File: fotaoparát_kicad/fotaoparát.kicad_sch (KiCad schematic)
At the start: 22 parts, among them J1 Conn_01x08_Pin, SW1 SW_MEC_5G, SW2 SW_MEC_5G, U1 TLV62569DBV, Y2 Crystal_GND23

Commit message: FInalni doteky. Ted uz jenom opravy {snad}
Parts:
- Y2: value Crystal_GND23 -> Crystal_GND24; LSCS Number (none) -> C5544483
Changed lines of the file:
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@@
 			)
 		)
-		(property "Value" "Crystal_GND23"
+		(property "Value" "Crystal_GND24"
 			(at 162.306 30.48 0)
 			(effects
@@
 			(at 148.59 29.21 0)
 			(effects
+				(font
+					(size 1.27 1.27)
+				)
+				(hide yes)
+			)
+		)
+		(property "LSCS Number" "C5544483"
+			(at 148.59 29.21 0)
+			(effects

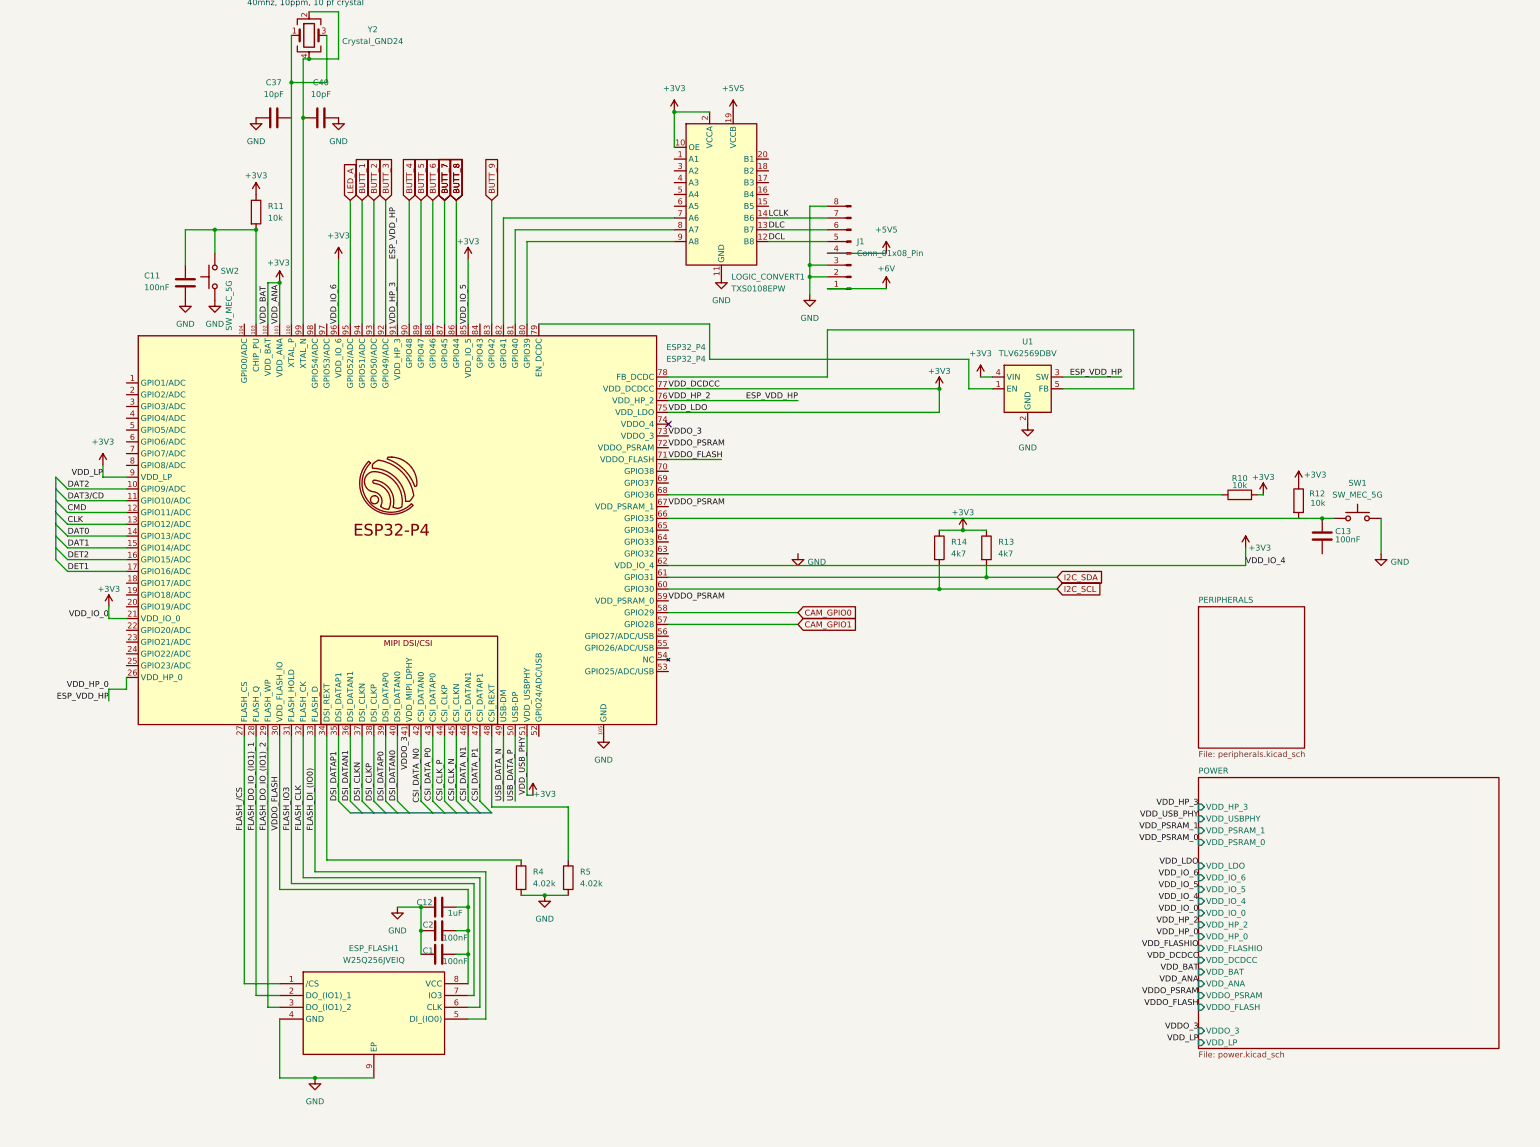
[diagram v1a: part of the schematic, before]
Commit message: Udelal jsem: -Predelani labelu na global -Pridani vyvodu na desku pro spoust -Pokusil se predelat ten stepdown, Vout by mela byt 1V1, nestihl jsem prepsat vsechny hodnoty a pridat lscs cisla
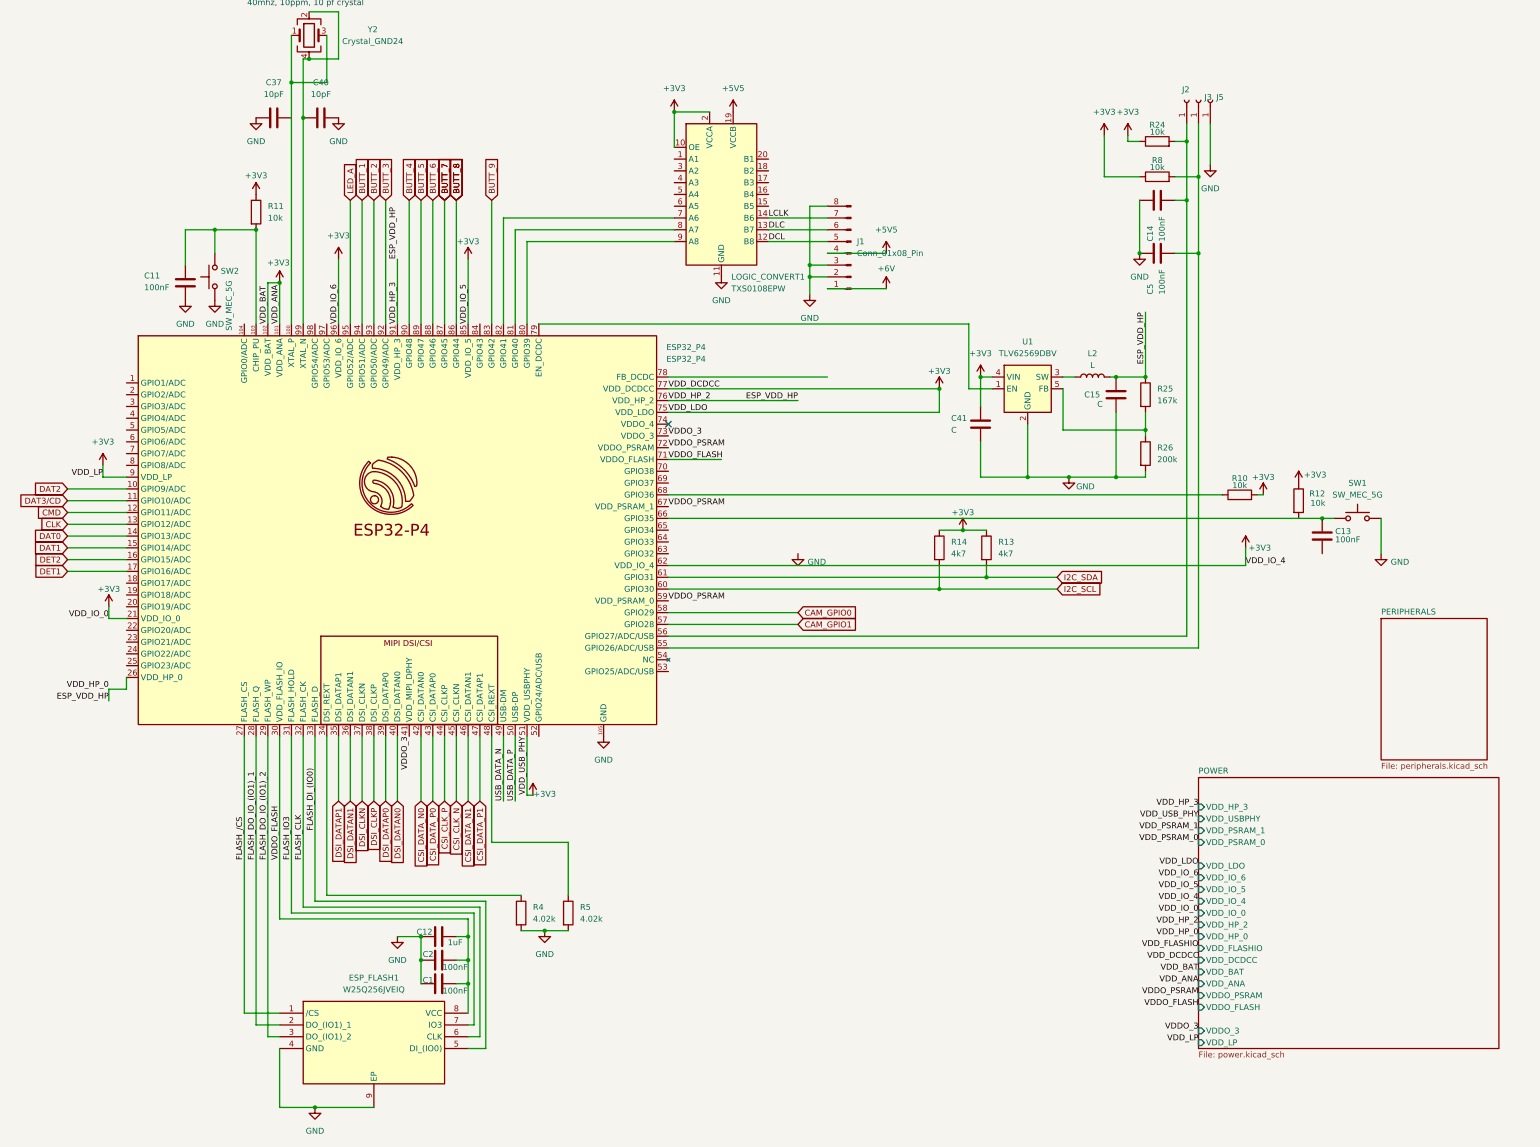
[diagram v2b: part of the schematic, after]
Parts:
- added C14, C5: 100nF, Capacitor_SMD:C_0201_0603Metric, symbol Device:C
- added C15, C41: C, symbol Device:C
- added J2, J3, J5: Conn_01x01_Socket, Connector_Wire:SolderWirePad_1x01_SMD_1.5x3mm, symbol Connector:Conn_01x01_Socket
- added L2: L, symbol Device:L
- added R24, R8: 10k, Resistor_SMD:R_0603_1608Metric, symbol Device:R
- added R25: 167k, symbol Device:R
- added R26: 200k, symbol Device:R
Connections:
- net +3V3: now also C41.1, R24.1, R8.1
- net ESP_VDD_HP: now also C15.1, L2.2, R25.1; no longer U1.3 (SW)
- net GND: now also C14.1, C15.2, C41.2, C5.1, J5.1 (Pin_1), R26.2
- net at ESP32_P4.55 (GPIO26/ADC/USB): now also C5.2, J3.1 (Pin_1), R8.2
- net at ESP32_P4.56 (GPIO27/ADC/USB): now also C14.2, J2.1 (Pin_1), R24.2
- net at U1.5 (FB): now also R25.2, R26.1; no longer ESP32_P4.78 (FB_DCDC)
- new net: L2.1, U1.3 (SW)
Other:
- moved on the sheet: C1, C12, C2, ESP_FLASH1, R4, R5

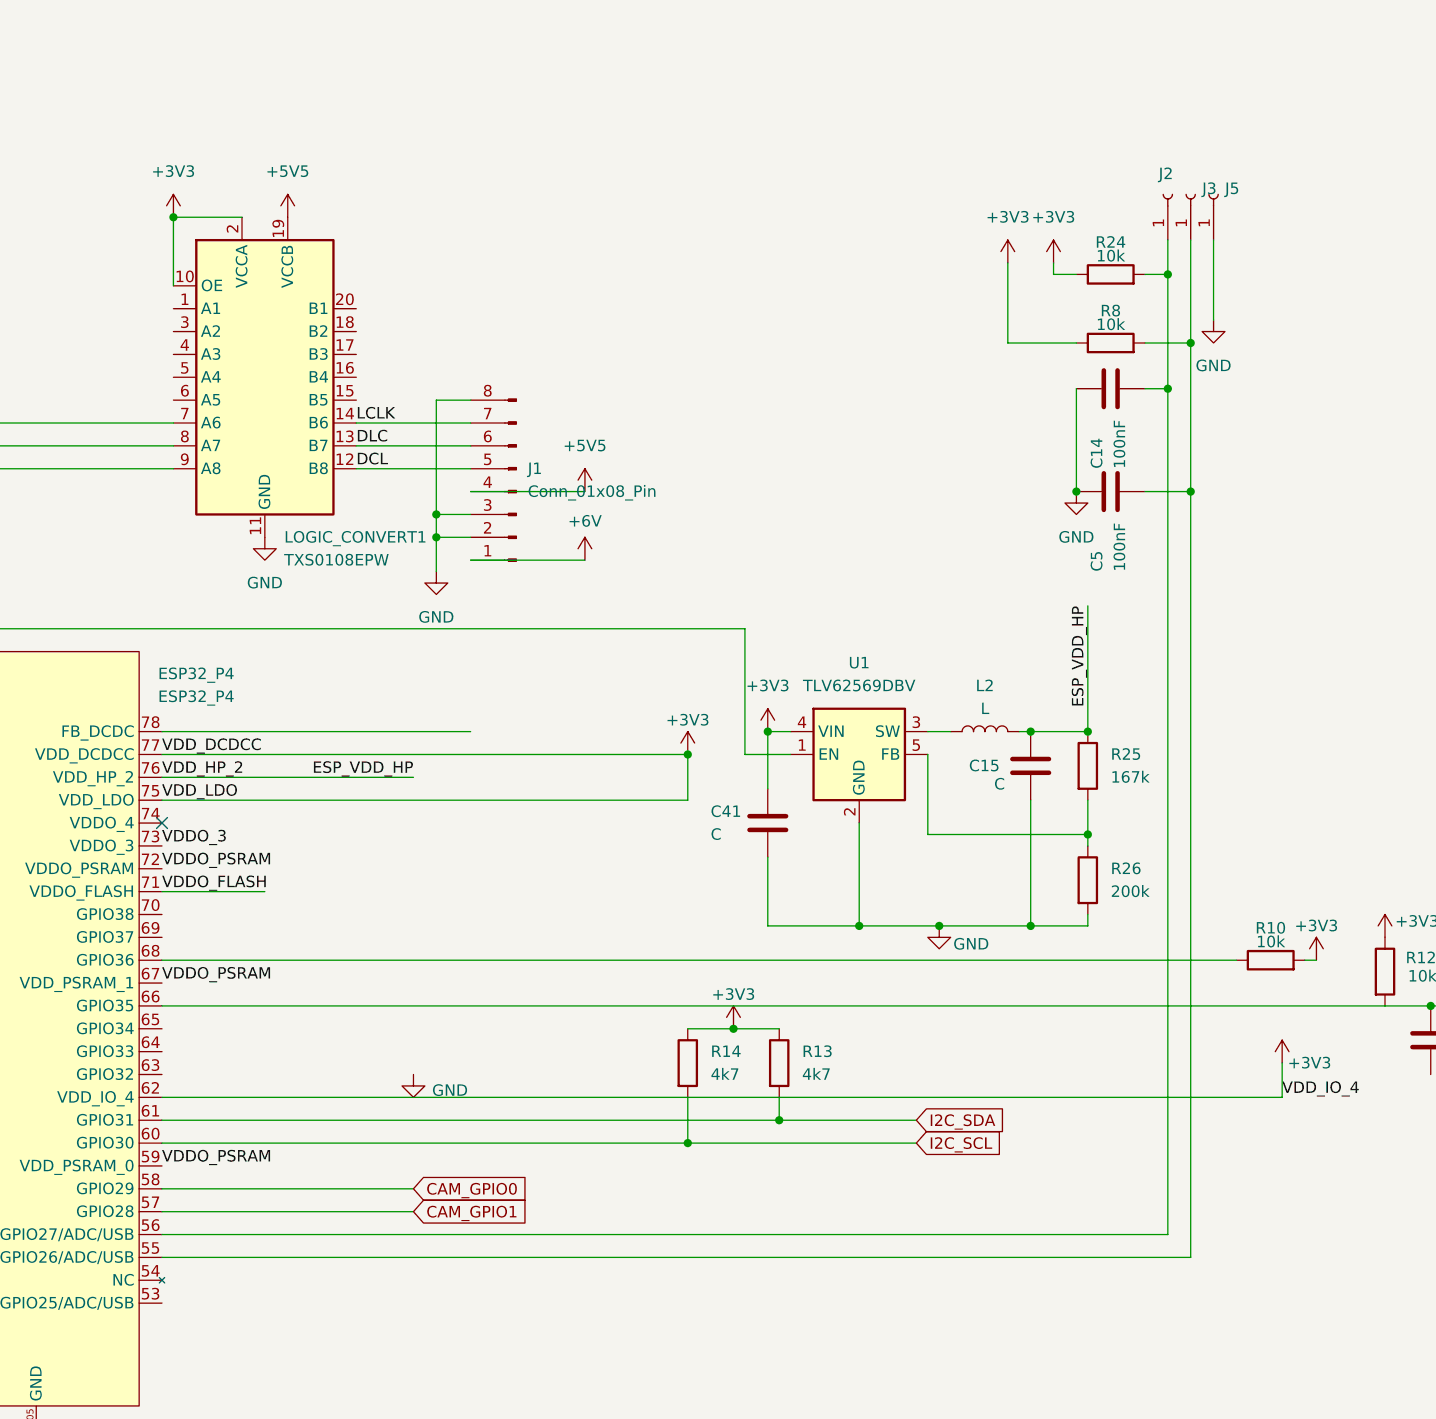
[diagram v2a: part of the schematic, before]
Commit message: Dodelani stepdownu, prirazeni lscs cisel
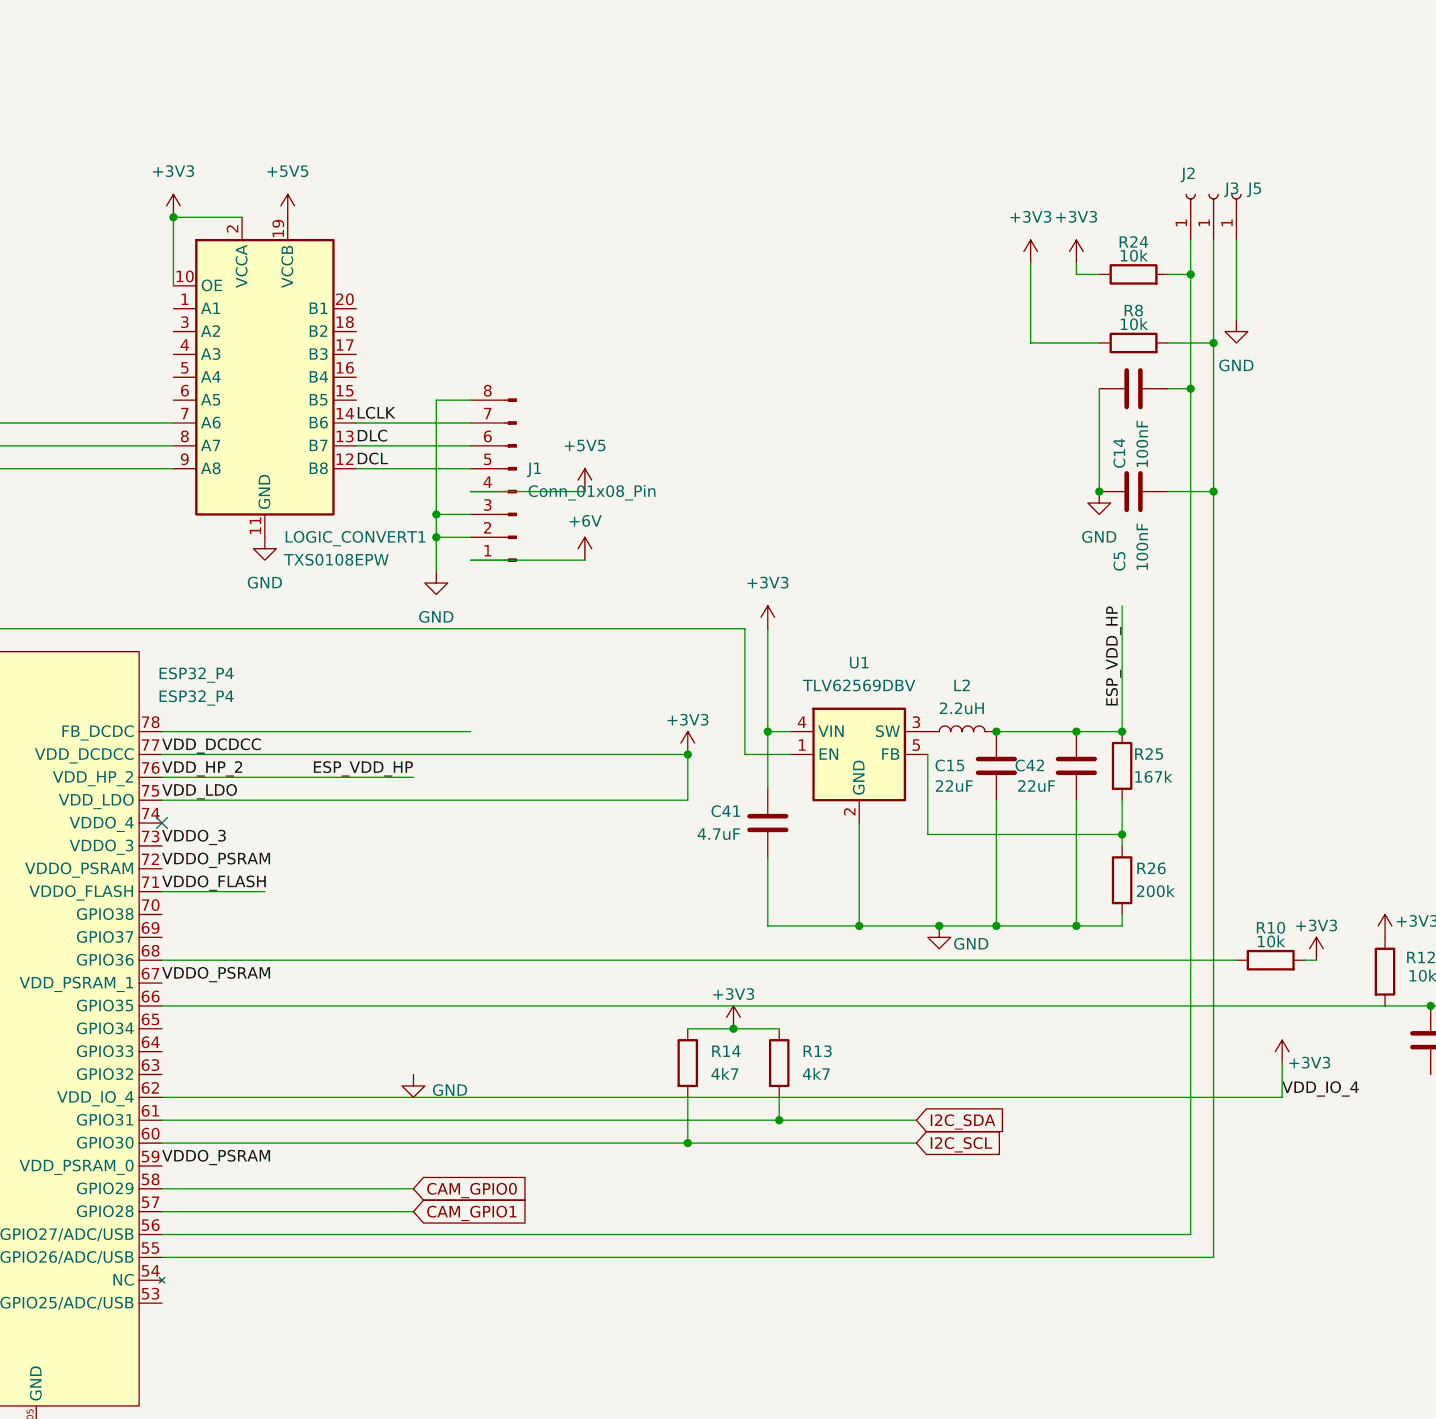
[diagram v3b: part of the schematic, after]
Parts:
- added C42: 22uF, Capacitor_SMD:C_0603_1608Metric, symbol Device:C
- C15: value C -> 22uF; footprint (none) -> Capacitor_SMD:C_0603_1608Metric; LSCS Number (none) -> C2762594
- C41: value C -> 4.7uF; footprint (none) -> Inductor_SMD:L_0603_1608Metric; LSCS Number (none) -> C19666
- L2: value L -> 2.2uH; footprint (none) -> Inductor_SMD:L_0603_1608Metric; LSCS Number (none) -> C394950
- R25: footprint (none) -> Resistor_SMD:R_0603_1608Metric; LSCS Number (none) -> C1727698
- R26: footprint (none) -> Resistor_SMD:R_0603_1608Metric; LSCS Number (none) -> C105574
- R4, R5: LSCS Number 0603 -> C23040
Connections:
- net ESP_VDD_HP: now also C42.1
- net GND: now also C42.2
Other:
- moved on the sheet: C14, C15, C5, J2, J3, J5, L2, R24, R25, R26, R8
